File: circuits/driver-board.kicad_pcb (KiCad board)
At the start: 4 copper layers, 40 x 47 mm, 74 parts, among them J1 Conn_01x18_Female, J2 USB4120-03-C_REVA, J3 Motor_Conn_01x04, J4 Screw_Terminals, J5 Conn_01x06_Female, Q1 SS8050-G, Q2 SS8050-G, SW1 RST_SW_Push, U1 CP2102N-Axx-xQFN24, U2 BA33DD0T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

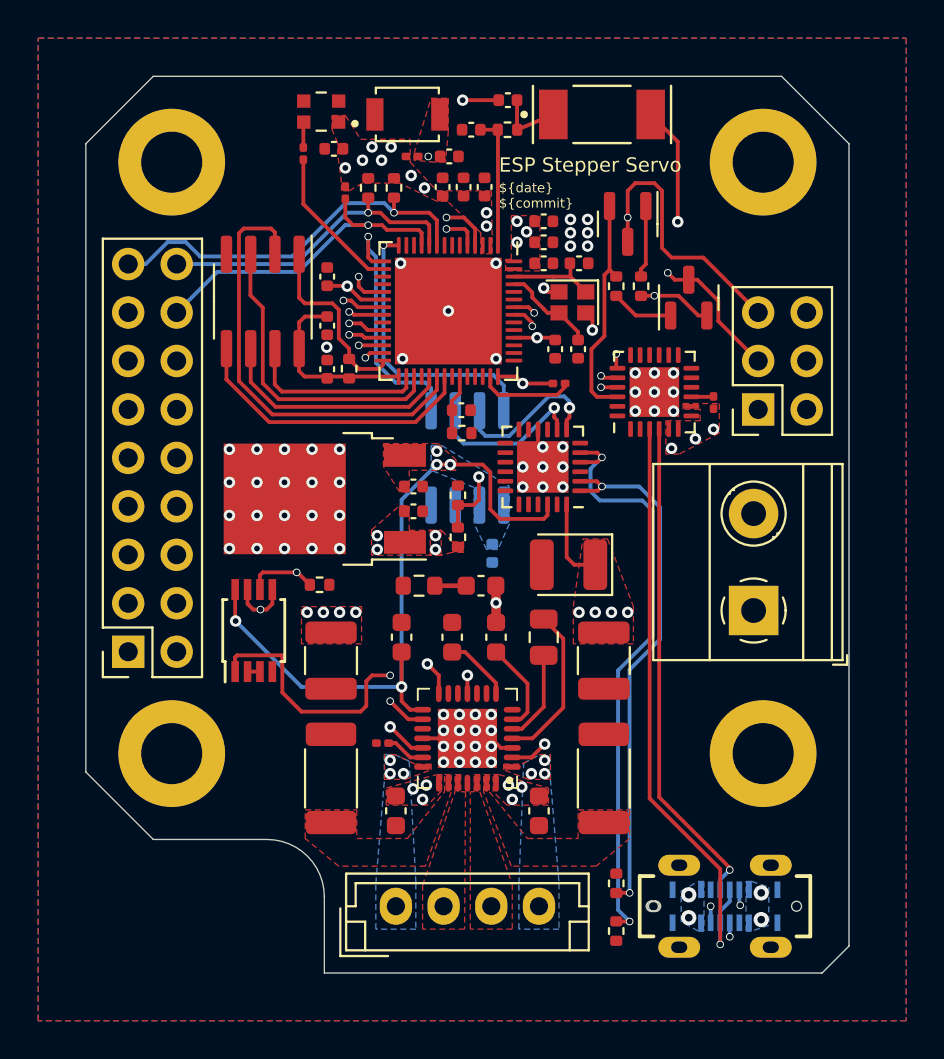
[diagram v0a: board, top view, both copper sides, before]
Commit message: updated groundplanes
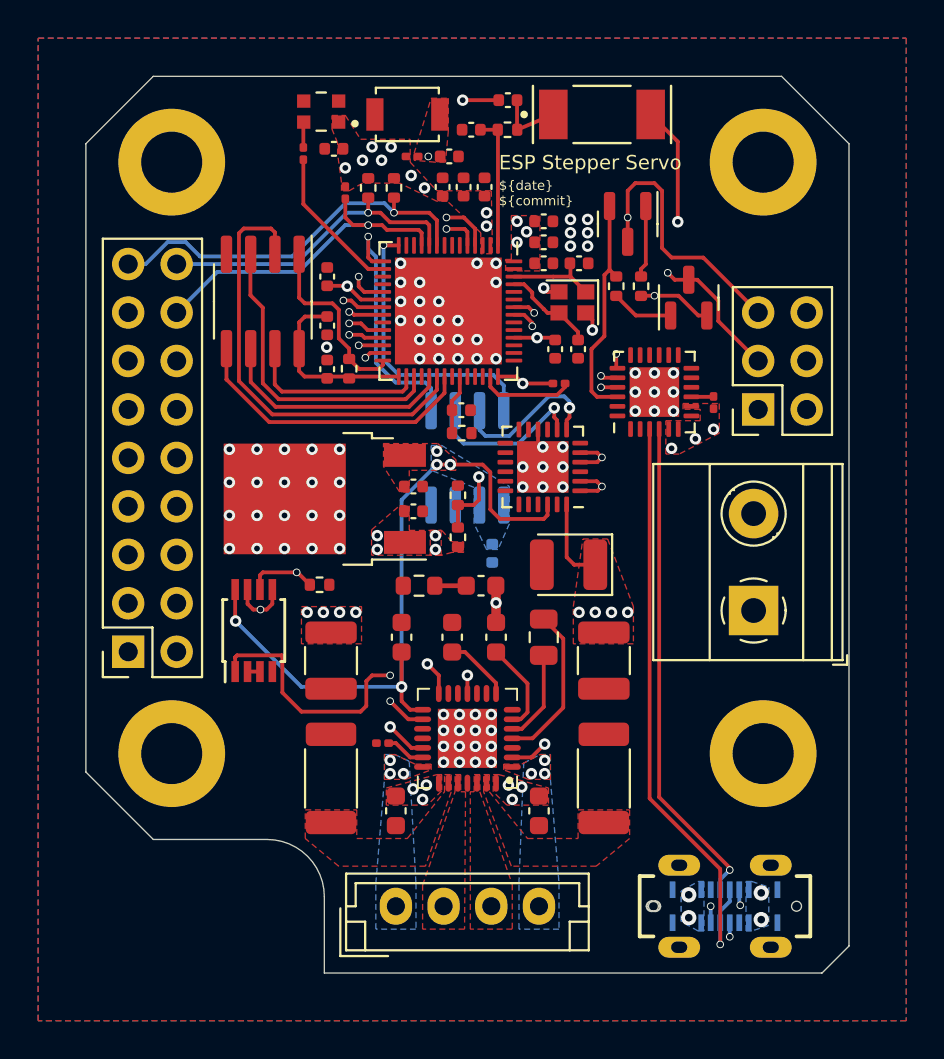
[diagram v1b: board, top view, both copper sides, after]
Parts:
- removed R10, R8: 5K1, Resistor_SMD:R_0402_1005Metric
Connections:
- J1 pad 13: GND -> unconnected-(J1-Pad13)
- J1 pad 15: unconnected-(J1-Pad15) -> GND
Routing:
- net /USB_CC1: track 37.0 -> 29.4 mm, vias 3 -> 2
- net /USB_CC2: track 37.5 -> 31.0 mm, vias 3 -> 2
- net GND: track 14.8 -> 11.3 mm, vias 69 -> 86
- added copper zone on In1.Cu, net GND

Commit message: changed gpio for step/dir
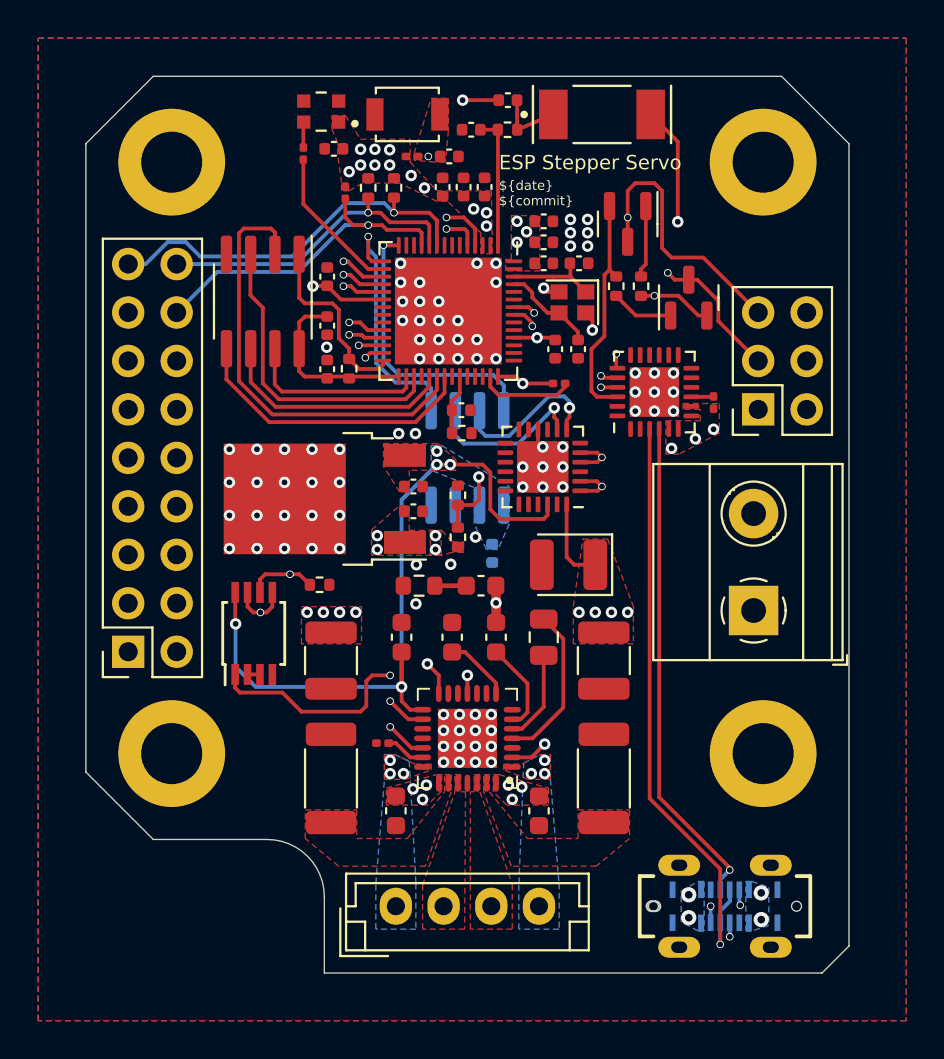
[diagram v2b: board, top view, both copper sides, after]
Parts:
- C10: value 100nF-50V-0603 -> 100nF
- C11: value 22nF-50V -> 22nF
- C12, C13: value 100nF-50V -> 100nF
- C15, C16: value 10µF-50V -> 10µF
- C3: value 10µF-35V -> 10µF
- C8: value 1µF-50V -> 1µF
- C9: value 2µ2F-6v3 -> 2.2µF
- R11: value 1K-1% -> 1K
- R3: value 0R100-0603 -> 0R100
- moved U8 0.15 mm to (38.8, 59.2)
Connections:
- H1 pad 1: (no net) -> GND
- H2 pad 1: (no net) -> GND
- H3 pad 1: (no net) -> GND
- H4 pad 1: (no net) -> GND
- J1 pad 13: unconnected-(J1-Pad13) -> +3V3
- U3 pad 17: /ESP_IO12 -> /TMC2209_DIR / ESP_IO12
- U3 pad 18: /ESP_IO13 -> /TMC2209_STEP / ESP_IO13
- U3 pad 21: /TMC2209_STEP / ESP_IO15 -> unconnected-(U3-Pad21)
- U3 pad 22: /TMC2209_DIR / ESP_IO16 -> unconnected-(U3-Pad22)
- U5 pad 16: /TMC2209_STEP / ESP_IO15 -> /TMC2209_STEP / ESP_IO13
- U5 pad 19: /TMC2209_DIR / ESP_IO16 -> /TMC2209_DIR / ESP_IO12
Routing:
- net /TMC2209_DIR / ESP_IO12: track 0.00 -> 32.6 mm, vias 0 -> 2
- net /TMC2209_STEP / ESP_IO13: track 0.00 -> 30.1 mm, vias 0 -> 2
- net /TMC2209_DIR / ESP_IO16: track 27.5 -> 0.00 mm, vias 2 -> 0
- net /TMC2209_STEP / ESP_IO15: track 27.3 -> 0.00 mm, vias 2 -> 0
- net +3V3: track 42.4 -> 44.4 mm, vias 22 -> 25
- net /TMC2209_DIAG: track 17.8 -> 15.9 mm
- net /VBUS_SENSE / ESP_IO14: track 18.6 -> 19.8 mm
- net /SR_Q / ESP_IO18: track 26.3 -> 25.5 mm
- net GND: vias 86 -> 92

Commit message: moved internal traces to back layer
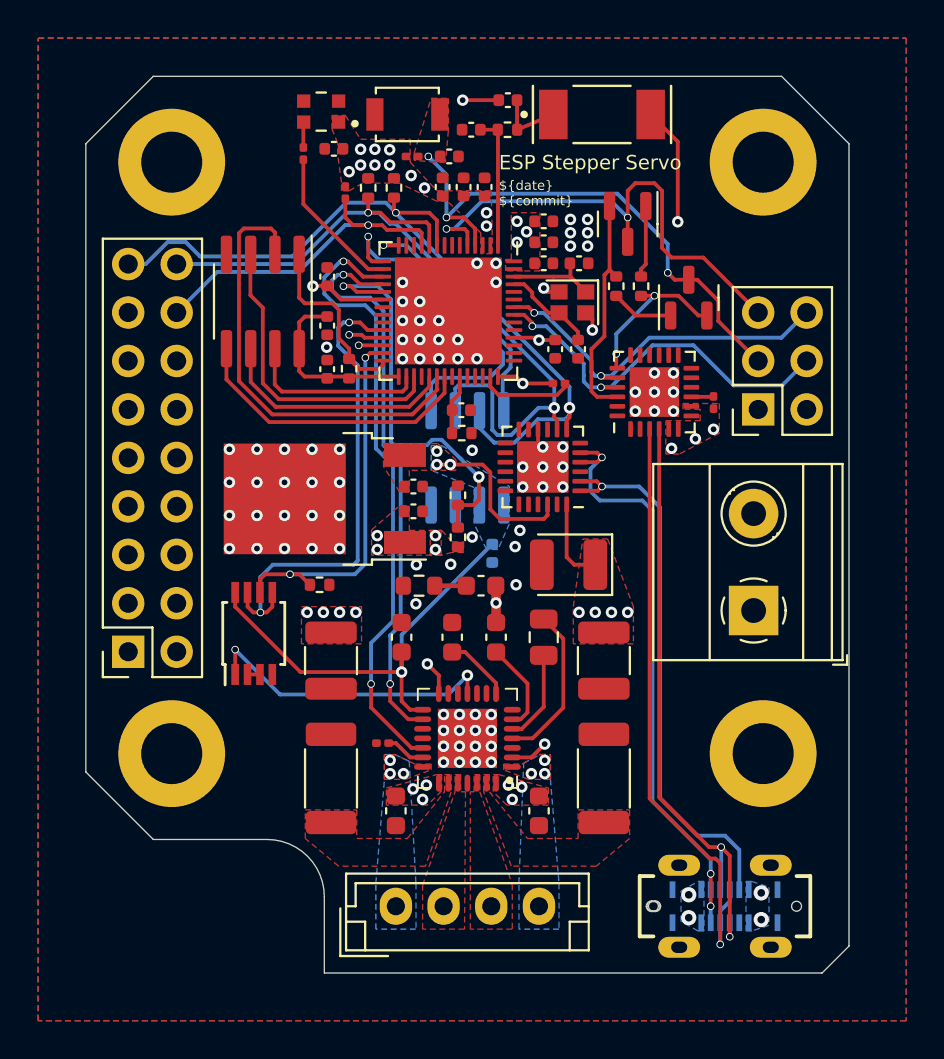
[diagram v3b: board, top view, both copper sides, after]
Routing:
- net +3V3: track 44.4 -> 38.5 mm, vias 25 -> 23
- net /AS5601_B_ITR / ESP_IO10: track 13.4 -> 18.1 mm
- net /I2C_SDA / ESP_IO05: track 39.8 -> 42.6 mm
- net /AS5601_A_ITR / ESP_IO09: track 15.0 -> 13.1 mm
- net /VBUS_SENSE / ESP_IO14: track 19.8 -> 21.6 mm
- net /USB_D-: track 30.1 -> 31.5 mm
- net /USB_CC1: track 29.4 -> 28.7 mm, vias 2 -> 1
- net GND: vias 92 -> 89
- net /USB_CC2: vias 2 -> 3
